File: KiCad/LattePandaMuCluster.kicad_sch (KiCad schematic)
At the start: 4 parts

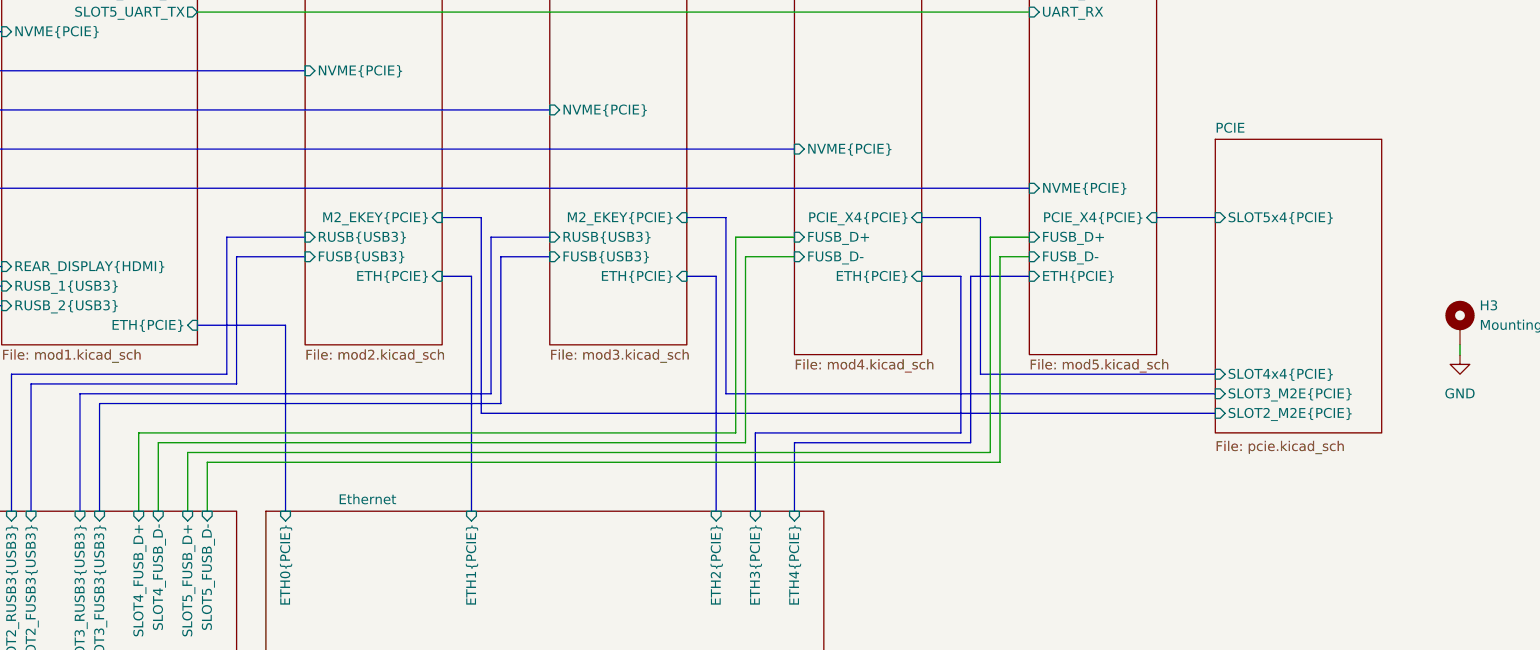
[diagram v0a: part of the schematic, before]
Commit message: Add PCIe x1 Slot
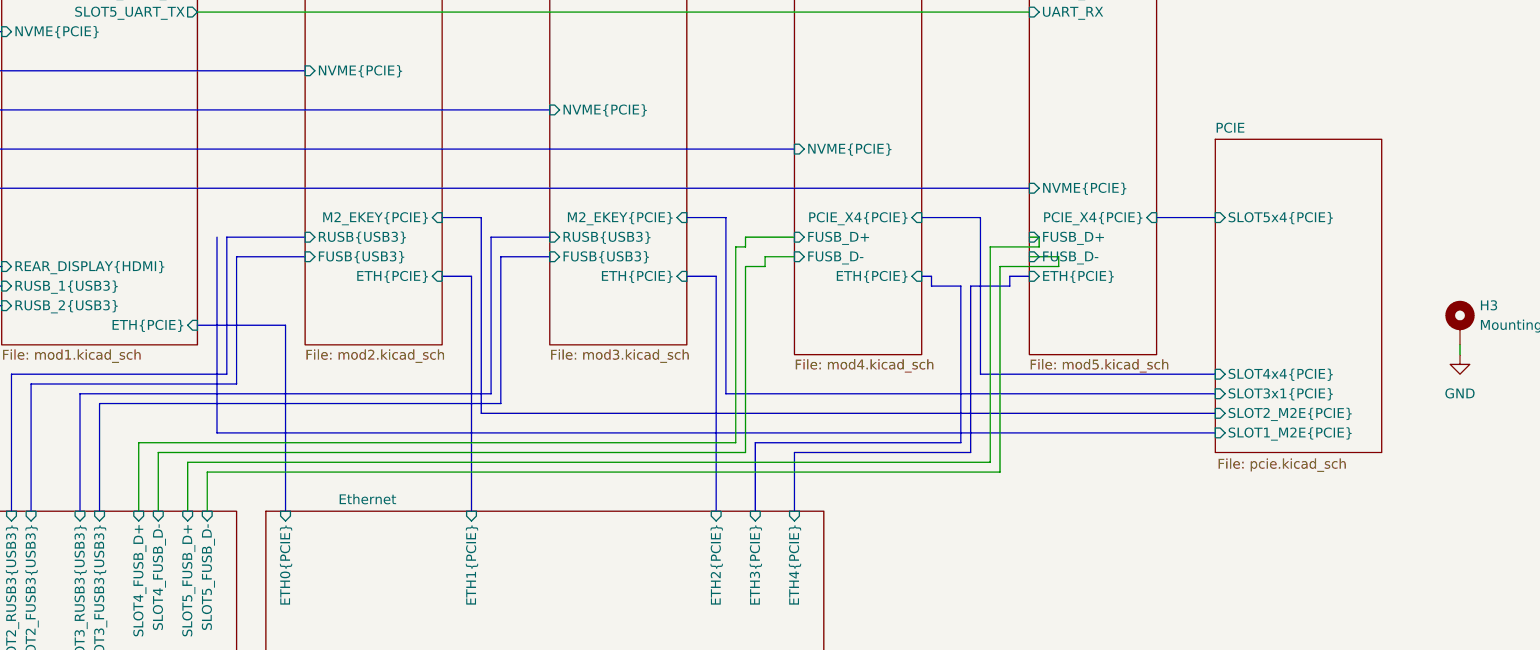
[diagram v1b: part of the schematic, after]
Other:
- sheet PCIE ports: added SLOT1_M2E{PCIE}, SLOT3x1{PCIE}; removed SLOT3_M2E{PCIE}
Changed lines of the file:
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@@
 	(wire
 		(pts
-			(xy 81.28 158.75) (xy 81.28 168.91)
+			(xy 81.28 160.02) (xy 81.28 168.91)
+		)
+		(stroke
+			(width 0)
+			(type default)
+		)
+	)
+	(wire
+		(pts
+			(xy 200.66 137.16) (xy 200.66 135.89)
 		)
 		(stroke
@@
 	(wire
 		(pts
-			(xy 158.75 158.75) (xy 81.28 158.75)
+			(xy 158.75 160.02) (xy 81.28 160.02)
 		)
 		(stroke
@@
 	(wire
 		(pts
-			(xy 166.37 133.35) (xy 158.75 133.35)
+			(xy 160.02 134.62) (xy 158.75 134.62)
 		)
 		(stroke
@@
 	(wire
 		(pts
-			(xy 191.77 161.29) (xy 87.63 161.29)
+			(xy 191.77 162.56) (xy 87.63 162.56)
 		)
 		(stroke
@@
 	(bus
 		(pts
-			(xy 196.85 138.43) (xy 189.23 138.43)
-		)
-		(stroke
-			(width 0)
-			(type default)
-		)
-	)
-	(bus
-		(pts
-			(xy 189.23 138.43) (xy 189.23 160.02)
+			(xy 194.31 139.7) (xy 189.23 139.7)
+		)
+		(stroke
+			(width 0)
+			(type default)
+		)
+	)
+	(bus
+		(pts
+			(xy 189.23 139.7) (xy 189.23 161.29)
 		)
 		(stroke
@@
 	(bus
 		(pts
+			(xy 184.15 139.7) (xy 184.15 138.43)
+		)
+		(stroke
+			(width 0)
+			(type default)
+		)
+	)
+	(bus
+		(pts
 			(xy 67.31 152.4) (xy 93.98 152.4)
 		)
@@
 	(bus
 		(pts
-			(xy 189.23 160.02) (xy 166.37 160.02)
+			(xy 189.23 161.29) (xy 166.37 161.29)
 		)
 		(stroke
@@
 	(bus
 		(pts
-			(xy 161.29 158.75) (xy 161.29 168.91)
+			(xy 161.29 160.02) (xy 161.29 168.91)
 		)
 		(stroke
@@
 	(bus
 		(pts
+			(xy 220.98 158.75) (xy 91.44 158.75)
+		)
+		(stroke
+			(width 0)
+			(type default)
+		)
+	)
+	(bus
+		(pts
 			(xy 100.33 144.78) (xy 100.33 168.91)
 		)
@@
 	(bus
 		(pts
+			(xy 91.44 133.35) (xy 91.44 158.75)
+		)
+		(stroke
+			(width 0)
+			(type default)
+		)
+	)
+	(bus
+		(pts
+			(xy 184.15 138.43) (xy 182.88 138.43)
+		)
+		(stroke
+			(width 0)
+			(type default)
+		)
+	)
+	(bus
+		(pts
 			(xy 190.5 130.81) (xy 190.5 151.13)
 		)
@@
 		)
 	)
+	(wire
+		(pts
+			(xy 160.02 134.62) (xy 160.02 133.35)
+		)
+		(stroke
+			(width 0)
+			(type default)
+		)
+	)
 	(bus
 		(pts
@@
 	(wire
 		(pts
-			(xy 196.85 135.89) (xy 193.04 135.89)
-		)
-		(stroke
-			(width 0)
-			(type default)
-		)
-	)
-	(bus
-		(pts
-			(xy 182.88 138.43) (xy 187.96 138.43)
+			(xy 200.66 137.16) (xy 193.04 137.16)
+		)
+		(stroke
+			(width 0)
+			(type default)
+		)
+	)
+	(bus
+		(pts
+			(xy 184.15 139.7) (xy 187.96 139.7)
 		)
 		(stroke
@@
 	(wire
 		(pts
+			(xy 198.12 133.35) (xy 196.85 133.35)
+		)
+		(stroke
+			(width 0)
+			(type default)
+		)
+	)
+	(wire
+		(pts
 			(xy 121.92 62.23) (xy 134.62 62.23)
 		)
@@
 	(bus
 		(pts
-			(xy 187.96 158.75) (xy 161.29 158.75)
-		)
-		(stroke
-			(width 0)
-			(type default)
-		)
-	)
-	(bus
-		(pts
-			(xy 187.96 138.43) (xy 187.96 158.75)
-		)
-		(stroke
-			(width 0)
-			(type default)
-		)
-	)
-	(wire
-		(pts
-			(xy 166.37 135.89) (xy 160.02 135.89)
+			(xy 187.96 160.02) (xy 161.29 160.02)
+		)
+		(stroke
+			(width 0)
+			(type default)
+		)
+	)
+	(bus
+		(pts
+			(xy 187.96 139.7) (xy 187.96 160.02)
+		)
+		(stroke
+			(width 0)
+			(type default)
+		)
+	)
+	(wire
+		(pts
+			(xy 162.56 137.16) (xy 160.02 137.16)
 		)
 		(stroke
@@
 	(wire
 		(pts
-			(xy 191.77 133.35) (xy 191.77 161.29)
+			(xy 191.77 134.62) (xy 191.77 162.56)
 		)
 		(stroke
@@
 		)
 	)
+	(wire
+		(pts
+			(xy 200.66 135.89) (xy 196.85 135.89)
+		)
+		(stroke
+			(width 0)
+			(type default)
+		)
+	)
 	(bus
 		(pts
@@
 	(wire
 		(pts
-			(xy 90.17 162.56) (xy 90.17 168.91)
+			(xy 90.17 163.83) (xy 90.17 168.91)
 		)
 		(stroke
@@
 	(wire
 		(pts
-			(xy 158.75 133.35) (xy 158.75 158.75)
+			(xy 158.75 134.62) (xy 158.75 160.02)
 		)
 		(stroke
@@
 		)
 	)
+	(wire
+		(pts
+			(xy 198.12 134.62) (xy 198.12 133.35)
+		)
+		(stroke
+			(width 0)
+			(type default)
+		)
+	)
 	(bus
 		(pts
@@
 	(wire
 		(pts
+			(xy 162.56 137.16) (xy 162.56 135.89)
+		)
+		(stroke
+			(width 0)
+			(type default)
+		)
+	)
+	(wire
+		(pts
 			(xy 85.09 52.07) (xy 218.44 52.07)
 		)
@@
 		)
 	)
+	(wire
+		(pts
+			(xy 160.02 133.35) (xy 166.37 133.35)
+		)
+		(stroke
+			(width 0)
+			(type default)
+		)
+	)
 	(bus
 		(pts
@@
 	(wire
 		(pts
-			(xy 193.04 162.56) (xy 90.17 162.56)
+			(xy 193.04 163.83) (xy 90.17 163.83)
 		)
 		(stroke
@@
 	(wire
 		(pts
-			(xy 160.02 160.02) (xy 83.82 160.02)
+			(xy 160.02 161.29) (xy 83.82 161.29)
 		)
 		(stroke
@@
 	(wire
 		(pts
-			(xy 83.82 160.02) (xy 83.82 168.91)
+			(xy 83.82 161.29) (xy 83.82 168.91)
 		)
 		(stroke
@@
 	(bus
 		(pts
+			(xy 194.31 138.43) (xy 196.85 138.43)
+		)
+		(stroke
+			(width 0)
+			(type default)
+		)
+	)
+	(bus
+		(pts
 			(xy 50.8 137.16) (xy 63.5 137.16)
 		)
@@
 		)
 	)
-	(wire
-		(pts
-			(xy 87.63 161.29) (xy 87.63 168.91)
+	(bus
+		(pts
+			(xy 194.31 139.7) (xy 194.31 138.43)
+		)
+		(stroke
+			(width 0)
+			(type default)
+		)
+	)
+	(wire
+		(pts
+			(xy 87.63 162.56) (xy 87.63 168.91)
 		)
 		(stroke
@@
 	(bus
 		(pts
-			(xy 166.37 160.02) (xy 166.37 168.91)
+			(xy 166.37 161.29) (xy 166.37 168.91)
 		)
 		(stroke
@@
 		)
 	)
+	(wire
+		(pts
+			(xy 162.56 135.89) (xy 166.37 135.89)
+		)
+		(stroke
+			(width 0)
+			(type default)
+		)
+	)
 	(bus
 		(pts
@@
 	(wire
 		(pts
-			(xy 193.04 135.89) (xy 193.04 162.56)
+			(xy 193.04 137.16) (xy 193.04 163.83)
 		)
 		(stroke
@@
 	(wire
 		(pts
-			(xy 160.02 135.89) (xy 160.02 160.02)
+			(xy 160.02 137.16) (xy 160.02 161.29)
 		)
 		(stroke
@@
 	(wire
 		(pts
-			(xy 196.85 133.35) (xy 191.77 133.35)
+			(xy 198.12 134.62) (xy 191.77 134.62)
 		)
 		(stroke
@@
 	(sheet
 		(at 220.98 120.65)
-		(size 21.59 38.1)
+		(size 21.59 40.64)
 		(exclude_from_sim no)
 		(in_bom yes)
@@
 		)
 		(property "Sheetfile" "pcie.kicad_sch"
-			(at 220.98 159.766 0)
+			(at 221.234 162.052 0)
 			(effects
 				(font
@@
 			)
 		)
-		(pin "SLOT3_M2E{PCIE}" input
-			(at 220.98 153.67 180)
-			(effects
-				(font
-					(size 1.27 1.27)
-				)
-				(justify left)
-			)
-		)
 		(pin "SLOT4x4{PCIE}" input
 			(at 220.98 151.13 180)
@@
 			(effects
 				(font
+					(size 1.27 1.27)
+				)
+				(justify left)
+			)
+		)
+		(pin "SLOT1_M2E{PCIE}" input
+			(at 220.98 158.75 180)
+			(effects
+				(font
+					(size 1.27 1.27)
+				)
+				(justify left)
+			)
+		)
+		(pin "SLOT3x1{PCIE}" input
+			(at 220.98 153.67 180)
+			(effects
+				(font

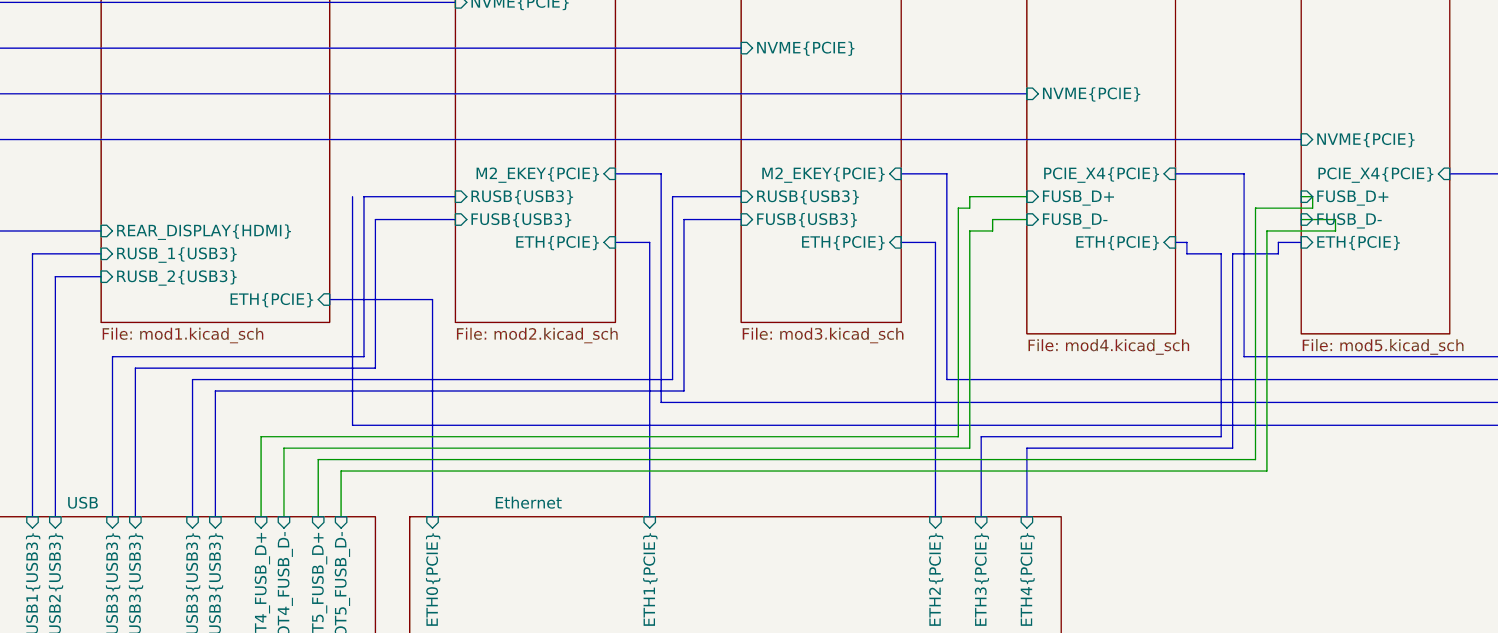
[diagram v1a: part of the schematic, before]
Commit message: Finish connecting x1 slot. Add pcie clkreq lines
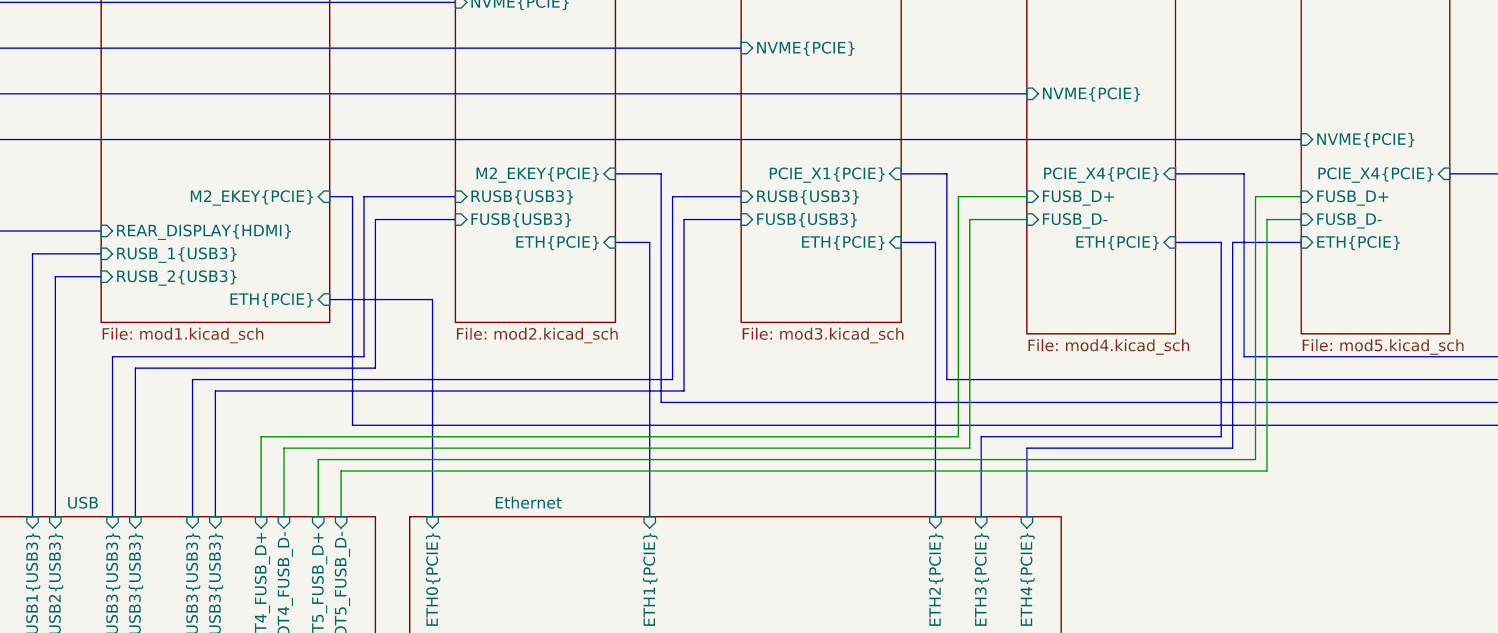
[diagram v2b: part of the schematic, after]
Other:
- sheet Module 1 ports: added M2_EKEY{PCIE}; removed none
- sheet Module 3 ports: added PCIE_X1{PCIE}; removed M2_EKEY{PCIE}
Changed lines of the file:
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@@
 	(wire
 		(pts
-			(xy 200.66 137.16) (xy 200.66 135.89)
+			(xy 193.04 135.89) (xy 193.04 163.83)
 		)
 		(stroke
@@
 	(wire
 		(pts
-			(xy 160.02 134.62) (xy 158.75 134.62)
+			(xy 158.75 133.35) (xy 166.37 133.35)
 		)
 		(stroke
@@
 	(bus
 		(pts
-			(xy 194.31 139.7) (xy 189.23 139.7)
+			(xy 189.23 138.43) (xy 196.85 138.43)
 		)
 		(stroke
@@
 	(bus
 		(pts
-			(xy 189.23 139.7) (xy 189.23 161.29)
+			(xy 189.23 138.43) (xy 189.23 161.29)
 		)
 		(stroke
@@
 	(bus
 		(pts
-			(xy 184.15 139.7) (xy 184.15 138.43)
-		)
-		(stroke
-			(width 0)
-			(type default)
-		)
-	)
-	(bus
-		(pts
 			(xy 67.31 152.4) (xy 93.98 152.4)
 		)
@@
 	(bus
 		(pts
-			(xy 184.15 138.43) (xy 182.88 138.43)
+			(xy 182.88 138.43) (xy 187.96 138.43)
 		)
 		(stroke
@@
 		)
 	)
-	(wire
-		(pts
-			(xy 160.02 134.62) (xy 160.02 133.35)
-		)
-		(stroke
-			(width 0)
-			(type default)
-		)
-	)
 	(bus
 		(pts
@@
 		)
 	)
-	(wire
-		(pts
-			(xy 200.66 137.16) (xy 193.04 137.16)
-		)
-		(stroke
-			(width 0)
-			(type default)
-		)
-	)
-	(bus
-		(pts
-			(xy 184.15 139.7) (xy 187.96 139.7)
-		)
-		(stroke
-			(width 0)
-			(type default)
-		)
-	)
 	(bus
 		(pts
@@
 	(wire
 		(pts
-			(xy 198.12 133.35) (xy 196.85 133.35)
+			(xy 191.77 133.35) (xy 196.85 133.35)
 		)
 		(stroke
@@
 	(bus
 		(pts
-			(xy 187.96 139.7) (xy 187.96 160.02)
+			(xy 187.96 138.43) (xy 187.96 160.02)
 		)
 		(stroke
@@
 	(wire
 		(pts
-			(xy 162.56 137.16) (xy 160.02 137.16)
+			(xy 160.02 135.89) (xy 166.37 135.89)
 		)
 		(stroke
@@
 		)
 	)
-	(wire
-		(pts
-			(xy 191.77 134.62) (xy 191.77 162.56)
-		)
-		(stroke
-			(width 0)
-			(type default)
-		)
-	)
 	(bus
 		(pts
@@
 	(wire
 		(pts
-			(xy 200.66 135.89) (xy 196.85 135.89)
+			(xy 193.04 135.89) (xy 196.85 135.89)
 		)
 		(stroke
@@
 	(wire
 		(pts
-			(xy 158.75 134.62) (xy 158.75 160.02)
+			(xy 158.75 133.35) (xy 158.75 160.02)
 		)
 		(stroke
@@
 	(wire
 		(pts
-			(xy 198.12 134.62) (xy 198.12 133.35)
+			(xy 191.77 133.35) (xy 191.77 162.56)
 		)
 		(stroke
@@
 	(wire
 		(pts
-			(xy 162.56 137.16) (xy 162.56 135.89)
-		)
-		(stroke
-			(width 0)
-			(type default)
-		)
-	)
-	(wire
-		(pts
 			(xy 85.09 52.07) (xy 218.44 52.07)
 		)
@@
 		)
 	)
-	(wire
-		(pts
-			(xy 160.02 133.35) (xy 166.37 133.35)
-		)
-		(stroke
-			(width 0)
-			(type default)
-		)
-	)
 	(bus
 		(pts
@@
 	(bus
 		(pts
-			(xy 194.31 138.43) (xy 196.85 138.43)
-		)
-		(stroke
-			(width 0)
-			(type default)
-		)
-	)
-	(bus
-		(pts
 			(xy 50.8 137.16) (xy 63.5 137.16)
 		)
@@
 		)
 	)
-	(bus
+	(wire
 		(pts
-			(xy 194.31 139.7) (xy 194.31 138.43)
+			(xy 87.63 162.56) (xy 87.63 168.91)
 		)
 		(stroke
@@
 		)
 	)
-	(wire
+	(bus
 		(pts
-			(xy 87.63 162.56) (xy 87.63 168.91)
+			(xy 88.9 133.35) (xy 91.44 133.35)
 		)
 		(stroke
@@
 		)
 	)
-	(wire
-		(pts
-			(xy 162.56 135.89) (xy 166.37 135.89)
-		)
-		(stroke
-			(width 0)
-			(type default)
-		)
-	)
 	(bus
 		(pts
@@
 		)
 	)
-	(wire
-		(pts
-			(xy 193.04 137.16) (xy 193.04 163.83)
-		)
-		(stroke
-			(width 0)
-			(type default)
-		)
-	)
 	(bus
 		(pts
@@
 	(wire
 		(pts
-			(xy 160.02 137.16) (xy 160.02 161.29)
+			(xy 160.02 135.89) (xy 160.02 161.29)
 		)
 		(stroke
@@
 		)
 	)
-	(wire
-		(pts
-			(xy 198.12 134.62) (xy 191.77 134.62)
-		)
-		(stroke
-			(width 0)
-			(type default)
-		)
-	)
 	(bus
 		(pts
@@
 			)
 		)
-		(pin "M2_EKEY{PCIE}" input
-			(at 152.4 130.81 0)
-			(effects
-				(font
-					(size 1.27 1.27)
-				)
-				(justify right)
-			)
-		)
 		(pin "RUSB{USB3}" input
 			(at 134.62 133.35 180)
@@
 			)
 		)
+		(pin "PCIE_X1{PCIE}" input
+			(at 152.4 130.81 0)
+			(effects
+				(font
+					(size 1.27 1.27)
+				)
+				(justify right)
+			)
+		)
 		(instances
 			(project "LattePandaMuCluster"
@@
 			)
 		)
+		(pin "M2_EKEY{PCIE}" input
+			(at 88.9 133.35 0)
+			(effects
+				(font
+					(size 1.27 1.27)
+				)
+				(justify right)
+			)
+		)
